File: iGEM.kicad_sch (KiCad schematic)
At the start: 33 parts, among them IC1 TMCS1107A1BQDRQ1, IC2 TMCS1107A1BQDRQ1, IC3 MCP4642-502E_UN, J1 Conn_01x02, J2 Conn_01x02, J3 Conn_01x02, J4 Conn_01x02, Q1 TIP122, Q2 TIP122, Q3 IRF4905, Q4 D44VH, Q5 IRF4905, Q6 D44VH, U1 ADC101C021CIMK, U2 ADC101C021CIMK, U3 PCA9536D, U4 ICL7667

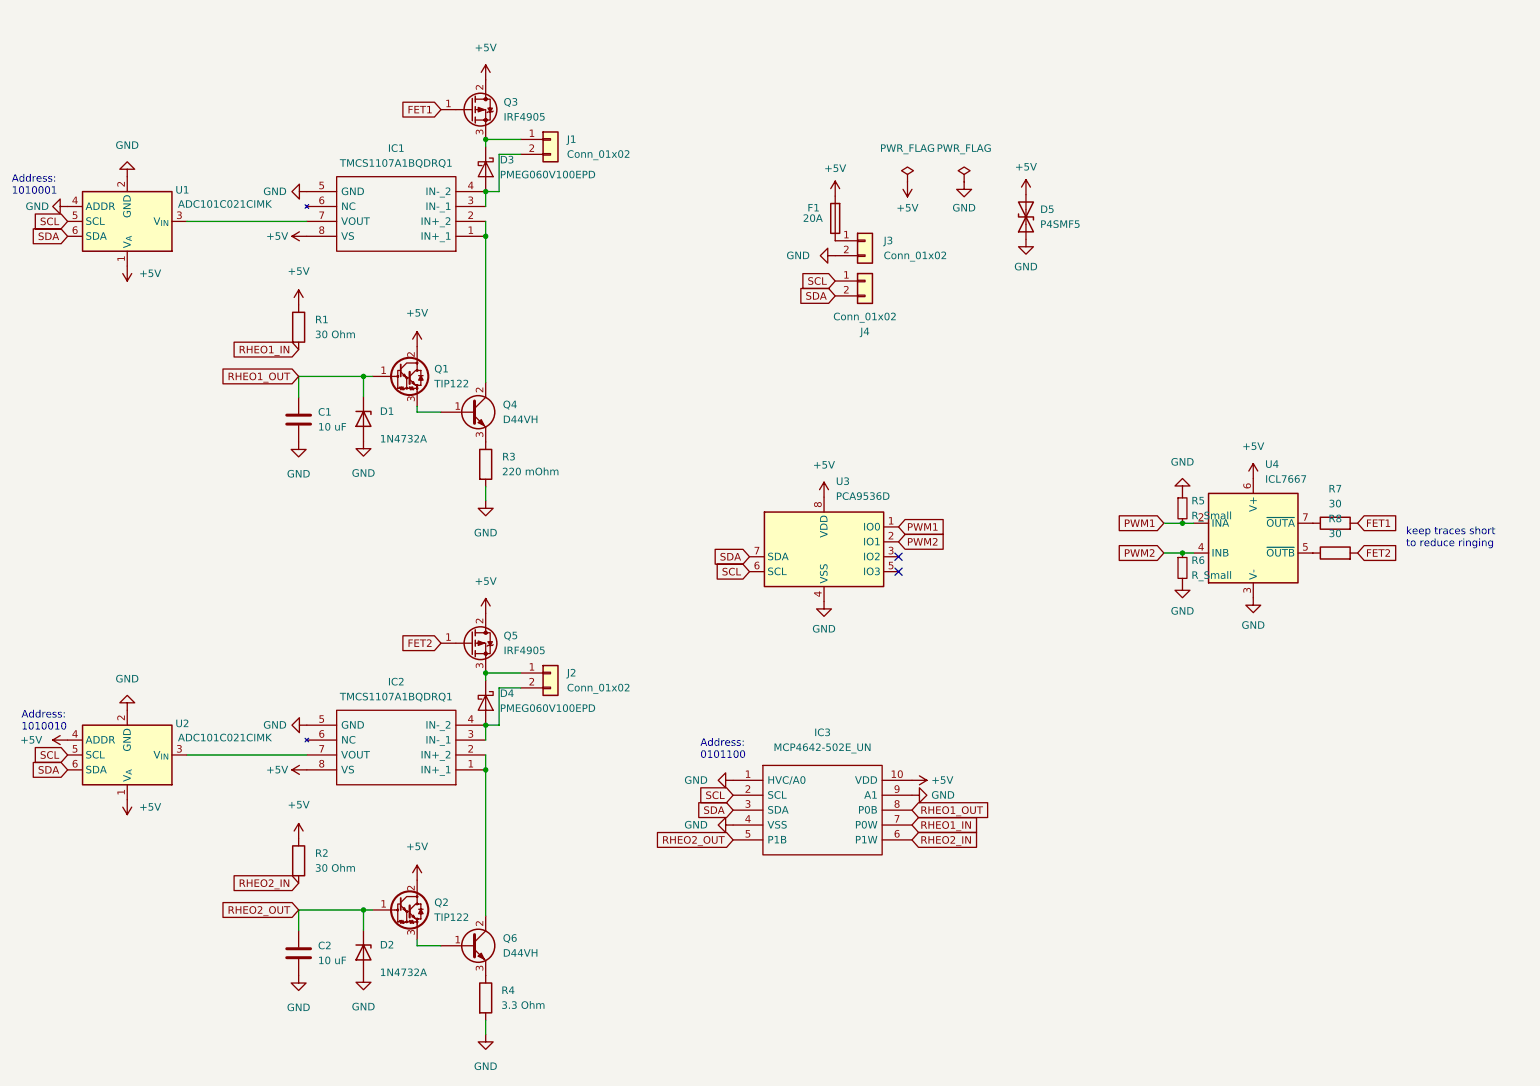
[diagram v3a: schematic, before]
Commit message: Schematics capture complete. Added footprints and DigiKey part numbers
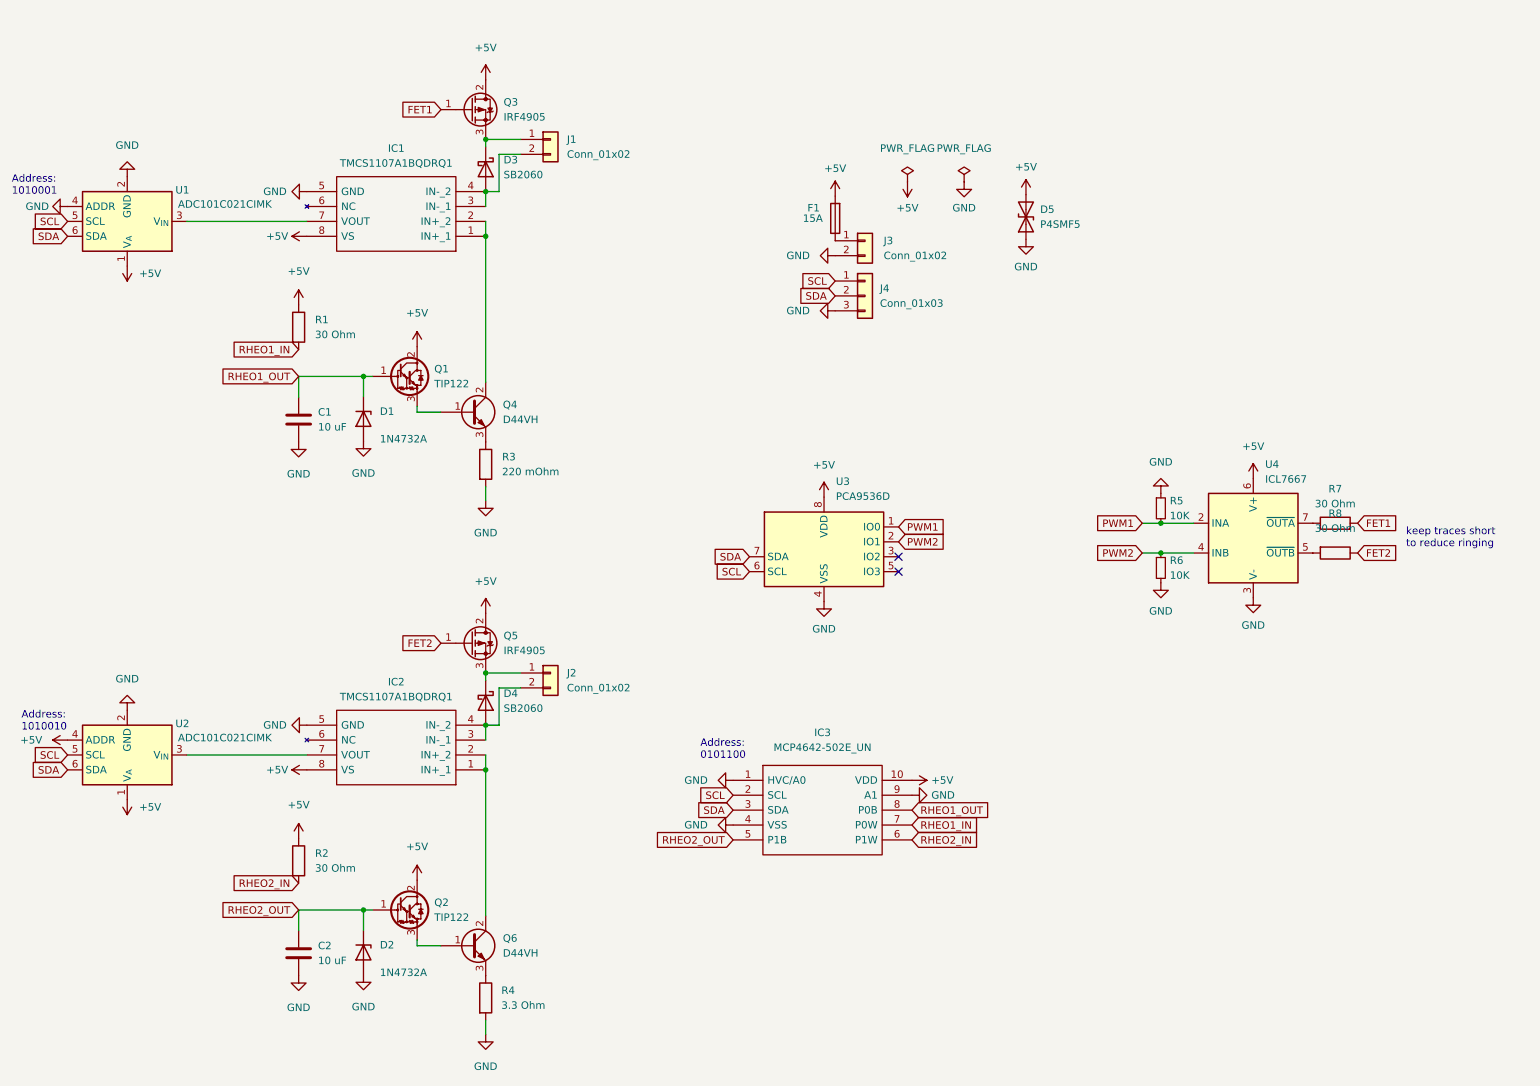
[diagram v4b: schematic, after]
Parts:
- removed D3, D4: PMEG060V100EPD, Package_TO_SOT_SMD:Nexperia_CFP15_SOT-1289, symbol Diode:PMEG060V100EPD
- removed J4: Conn_01x02, symbol Connector_Generic:Conn_01x02
- added D3, D4: SB2060, Diode_THT:D_DO-201AD_P15.24mm_Horizontal, symbol Device:D_Schottky
- added J4: Conn_01x03, Connector_JST:JST_XH_B3B-XH-AM_1x03_P2.50mm_Vertical, symbol Connector_Generic:Conn_01x03
- C1, C2: footprint (none) -> Capacitor_SMD:C_0805_2012Metric_Pad1.18x1.45mm_HandSolder; DigiKey (none) -> 399-C0805C106K8PAC7800CT-ND
- D1, D2: DigiKey (none) -> 1N4732AFSCT-ND
- D5: footprint (none) -> Diode_SMD:D_SOD-123F; DigiKey (none) -> 1655-P4SMF5.0CACT-ND
- F1: value 20A -> 15A; footprint (none) -> Fuse:Fuseholder_Blade_Mini_Keystone_3568; DigiKey (none) -> 36-3568-15-ND
- IC1: footprint TMCS1107A1BQDRQ1:SOIC127P600X175-8N -> Package_SO:SOIC-8_3.9x4.9mm_P1.27mm; DigiKey (none) -> 296-TMCS1107A1BQDRQ1CT-ND
- IC2: DigiKey (none) -> 296-TMCS1107A1BQDRQ1CT-ND
- IC3: DigiKey (none) -> MCP4642-502E/UN-ND
- J1, J2: footprint (none) -> TerminalBlock:TerminalBlock_bornier-2_P5.08mm; DigiKey (none) -> 102-6218-ND
- J3: footprint (none) -> 8PCV-02-006:8PCV02006; DigiKey (none) -> A98460-ND
- Q1, Q2: DigiKey (none) -> TIP122GOS-ND
- Q3, Q5: DigiKey (none) -> IRF4905PBF-ND
- Q4, Q6: DigiKey (none) -> D44VH10GOS-ND
- R1, R2: footprint (none) -> Capacitor_SMD:C_0805_2012Metric_Pad1.18x1.45mm_HandSolder; DigiKey (none) -> RMCF0805FT30R0CT-ND
- R3: footprint (none) -> TerminalBlock:TerminalBlock_bornier-2_P5.08mm; DigiKey (none) -> A102180-ND
- R4: footprint (none) -> TerminalBlock:TerminalBlock_bornier-2_P5.08mm; DigiKey (none) -> A102423-ND
- R5, R6: value R_Small -> 10K; footprint (none) -> Capacitor_SMD:C_0805_2012Metric_Pad1.18x1.45mm_HandSolder; DigiKey (none) -> RMCF0805FT10K0CT-ND
- R7, R8: value 30 -> 30 Ohm; footprint (none) -> Capacitor_SMD:C_0805_2012Metric_Pad1.18x1.45mm_HandSolder; DigiKey (none) -> RMCF0805FT30R0CT-ND
- U1, U2: DigiKey (none) -> ADC101C021CIMK/NOPBCT-ND
- U3: DigiKey (none) -> 296-21765-1-ND
- U4: footprint (none) -> Package_SO:SOIC-8_3.9x4.9mm_P1.27mm; DigiKey (none) -> ICL7667EBA+-ND
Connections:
- net FET2: now also R8.1; no longer R8.2
- net GND: now also J4.3 (Pin_3)
- net SCL: now also J4.1 (Pin_1)
- net SDA: now also J4.2 (Pin_2)
- net at J1.1 (Pin_1), Q3.3 (S): now also D3.1 (K)
- net at IC1.3 (IN-_1), IC1.4 (IN-_2), J1.2 (Pin_2): now also D3.2 (A)
- net at IC2.3 (IN-_1), IC2.4 (IN-_2), J2.2 (Pin_2): now also D4.2 (A)
- net at J2.1 (Pin_1), Q5.3 (S): now also D4.1 (K)
- net at U4.5 (~{OUTB}): now also R8.2; no longer R8.1
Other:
- moved on the sheet: R5, R6, R8

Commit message: layout draft complete
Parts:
- removed D5: P4SMF5, Diode_SMD:D_SOD-123F, symbol Device:D_TVS
- added C10, C6, C7, C8: 4.7 uF, Capacitor_Tantalum_SMD:CP_EIA-3528-21_Kemet-B_Pad1.50x2.35mm_HandSolder, symbol Device:C_Polarized
- added C11, C3, C4, C5, C9: 0.1 uF, Capacitor_SMD:C_0805_2012Metric_Pad1.18x1.45mm_HandSolder, symbol Device:C
- added H1, H2, H3, H4: MH, MountingHole:MountingHole_5.3mm_M5_DIN965_Pad, symbol Mechanical:MountingHole_Pad
- added HS1, HS2: Heatsink, Heatsink:Heatsink_AAVID_576802B03900G, symbol Mechanical:Heatsink_Pad
- added M1: Fan, Connector_JST:JST_XH_B2B-XH-AM_1x02_P2.50mm_Vertical, symbol Motor:Fan
- added R10, R9: 5K, Resistor_SMD:R_0805_2012Metric_Pad1.20x1.40mm_HandSolder, symbol Device:R
- C1, C2: value 10 uF -> 0.1 uF; DigiKey 399-C0805C106K8PAC7800CT-ND -> (none)
- D3, D4: footprint Diode_THT:D_DO-201AD_P15.24mm_Horizontal -> Diode_THT:D_DO-201AD_P12.70mm_Horizontal
- J4: DigiKey 455-2250-ND -> 455-2231-ND
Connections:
- net +5V: now also C1.1, C2.1, C10.1, C11.1, C3.1, C4.1, C5.1, C6.1, C7.1, C8.1, C9.1, M1.1 (+), R10.1, R9.1
- net GND: now also C10.2, C11.2, C3.2, C4.2, C5.2, C6.2, C7.2, C8.2, C9.2, H1.1, H2.1, H3.1, H4.1, M1.2 (-)
- net RHEO1_OUT: no longer C1.1
- net RHEO2_OUT: no longer C2.1
- net SCL: now also R9.2
- net SDA: now also R10.2
- net at D3.2 (A), J1.2 (Pin_2): now also IC1.1 (IN+_1), IC1.2 (IN+_2); no longer IC1.3 (IN-_1), IC1.4 (IN-_2)
- net at IC2.1 (IN+_1), IC2.2 (IN+_2): now also D4.2 (A), J2.2 (Pin_2); no longer Q6.2 (C)
- net at IC2.3 (IN-_1), IC2.4 (IN-_2): now also Q6.2 (C), HS2.1; no longer D4.2 (A), J2.2 (Pin_2)
- new net: HS1.1, IC1.3 (IN-_1), IC1.4 (IN-_2), Q4.2 (C)
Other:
- moved on the sheet: F1, IC1, IC2, IC3, J3, J4, U1, U2

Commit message: updated DigiKey part numbers and value of i2c pullups
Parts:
- C1, C11, C2, C3, C4, C5, C9: DigiKey (none) -> 399-C0805C104K8RAC7800CT-ND
- M1: DigiKey (none) -> 455-2879-ND
- R10, R9: value 5K -> 4.7K; DigiKey (none) -> RMCF0805FT4K70CT-ND
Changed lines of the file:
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@@
+      (effects (font (size 1.27 1.27)) hide)
+    )
+    (property "DigiKey" "399-C0805C104K8RAC7800CT-ND" (id 4) (at 172.466 88.773 0)
       (effects (font (size 1.27 1.27)) hide)
     )
@@
       (effects (font (size 1.27 1.27)) (justify left))
     )
-    (property "Value" "5K" (id 1) (at 255.778 51.8159 0)
+    (property "Value" "4.7K" (id 1) (at 255.778 51.8159 0)
       (effects (font (size 1.27 1.27)) (justify left))
     )
@@
     )
     (property "Datasheet" "~" (id 3) (at 253.873 50.546 0)
+      (effects (font (size 1.27 1.27)) hide)
+    )
+    (property "DigiKey" "RMCF0805FT4K70CT-ND" (id 4) (at 253.873 50.546 0)
       (effects (font (size 1.27 1.27)) hide)
     )
@@
     )
     (property "Datasheet" "~" (id 3) (at 242.443 82.169 0)
+      (effects (font (size 1.27 1.27)) hide)
+    )
+    (property "DigiKey" "399-C0805C104K8RAC7800CT-ND" (id 4) (at 242.443 82.169 0)
       (effects (font (size 1.27 1.27)) hide)
     )
@@
       (effects (font (size 1.27 1.27)) (justify left))
     )
-    (property "Value" "5K" (id 1) (at 263.017 51.8159 0)
+    (property "Value" "4.7K" (id 1) (at 263.017 51.8159 0)
       (effects (font (size 1.27 1.27)) (justify left))
     )
@@
     )
     (property "Datasheet" "~" (id 3) (at 260.35 50.546 0)
+      (effects (font (size 1.27 1.27)) hide)
+    )
+    (property "DigiKey" "RMCF0805FT4K70CT-ND" (id 4) (at 260.35 50.546 0)
       (effects (font (size 1.27 1.27)) hide)
     )
@@
       (effects (font (size 1.27 1.27)) hide)
     )
+    (property "DigiKey" "399-C0805C104K8RAC7800CT-ND" (id 4) (at 259.715 135.382 0)
+      (effects (font (size 1.27 1.27)) hide)
+    )
     (pin "1")
     (pin "2")
@@
     )
     (property "Datasheet" "~" (id 3) (at 128.905 31.369 0)
+      (effects (font (size 1.27 1.27)) hide)
+    )
+    (property "DigiKey" "399-C0805C104K8RAC7800CT-ND" (id 4) (at 128.905 31.369 0)
       (effects (font (size 1.27 1.27)) hide)
     )
@@
       (effects (font (size 1.27 1.27)) hide)
     )
+    (property "DigiKey" "399-C0805C104K8RAC7800CT-ND" (id 4) (at 128.651 122.174 0)
+      (effects (font (size 1.27 1.27)) hide)
+    )
     (pin "1")
     (pin "2")
@@
       (effects (font (size 1.27 1.27)) hide)
     )
+    (property "DigiKey" "455-2879-ND" (id 4) (at 263.398 27.178 0)
+      (effects (font (size 1.27 1.27)) hide)
+    )
     (pin "1")
     (pin "2")
@@
       (effects (font (size 1.27 1.27)) hide)
     )
+    (property "DigiKey" "399-C0805C104K8RAC7800CT-ND" (id 4) (at 179.197 123.444 0)
+      (effects (font (size 1.27 1.27)) hide)
+    )
     (pin "1")
     (pin "2")
@@
     )
     (property "Datasheet" "~" (id 3) (at 179.197 32.131 0)
+      (effects (font (size 1.27 1.27)) hide)
+    )
+    (property "DigiKey" "399-C0805C104K8RAC7800CT-ND" (id 4) (at 179.197 32.131 0)
       (effects (font (size 1.27 1.27)) hide)
     )
@@
     )
     (path "/1077e872-3c2a-4d54-b8f8-6275676956e2"
-      (reference "R9") (unit 1) (value "5K") (footprint "Resistor_SMD:R_0805_2012Metric_Pad1.20x1.40mm_HandSolder")
+      (reference "R9") (unit 1) (value "4.7K") (footprint "Resistor_SMD:R_0805_2012Metric_Pad1.20x1.40mm_HandSolder")
     )
     (path "/3f4af9bf-6e51-4fa2-939e-94b56f8a6a0c"
-      (reference "R10") (unit 1) (value "5K") (footprint "Resistor_SMD:R_0805_2012Metric_Pad1.20x1.40mm_HandSolder")
+      (reference "R10") (unit 1) (value "4.7K") (footprint "Resistor_SMD:R_0805_2012Metric_Pad1.20x1.40mm_HandSolder")
     )
     (path "/69a61c1d-1543-4184-a789-f583b0735f7e"

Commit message: Added PCA9536D address
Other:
- note added: "Address: 1000001"
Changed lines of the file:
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@@
     (stroke (width 0) (type default) (color 0 0 0 0))
+  )
+  (text "Address:\n1000001" (at 145.034 97.409 0)
+    (effects (font (size 1.27 1.27)) (justify left bottom))
   )
   (text "keep traces short\nto reduce ringing" (at 255.778 105.029 0)

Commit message: mounting holes no longer connected to signal ground because the chassis will be connected to true earth
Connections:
- net GND: no longer H1.1, H2.1, H3.1, H4.1
- no-connect marks 2 -> 6
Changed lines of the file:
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@@
   (junction (at 78.105 75.692) (diameter 0) (color 0 0 0 0)
   )
+  (no_connect (at 220.98 24.511))
+  (no_connect (at 228.727 24.638))
+  (no_connect (at 236.093 24.638))
+  (no_connect (at 243.84 24.765))
   (no_connect (at 169.291 106.426))
   (no_connect (at 169.291 108.966))
@@
     (pin "2")
     (pin "3")
-  )
-  (symbol (lib_id "power:GND") (at 220.98 24.511 0) (unit 1)
-    (in_bom yes) (on_board yes) (fields_autoplaced)
-    (property "Reference" "#PWR08" (id 0) (at 220.98 30.861 0)
-      (effects (font (size 1.27 1.27)) hide)
-    )
-    (property "Value" "GND" (id 1) (at 220.98 29.21 0))
-    (property "Footprint" "" (id 2) (at 220.98 24.511 0)
-      (effects (font (size 1.27 1.27)) hide)
-    )
-    (property "Datasheet" "" (id 3) (at 220.98 24.511 0)
-      (effects (font (size 1.27 1.27)) hide)
-    )
-    (pin "1")
-  )
-  (symbol (lib_id "power:GND") (at 243.84 24.765 0) (unit 1)
-    (in_bom yes) (on_board yes) (fields_autoplaced)
-    (property "Reference" "#PWR030" (id 0) (at 243.84 31.115 0)
-      (effects (font (size 1.27 1.27)) hide)
-    )
-    (property "Value" "GND" (id 1) (at 243.84 29.464 0))
-    (property "Footprint" "" (id 2) (at 243.84 24.765 0)
-      (effects (font (size 1.27 1.27)) hide)
-    )
-    (property "Datasheet" "" (id 3) (at 243.84 24.765 0)
-      (effects (font (size 1.27 1.27)) hide)
-    )
-    (pin "1")
   )
   (symbol (lib_id "power:GND") (at 156.591 114.046 0) (unit 1)
@@
     (pin "1")
   )
-  (symbol (lib_id "power:GND") (at 228.727 24.638 0) (unit 1)
-    (in_bom yes) (on_board yes) (fields_autoplaced)
-    (property "Reference" "#PWR010" (id 0) (at 228.727 30.988 0)
-      (effects (font (size 1.27 1.27)) hide)
-    )
-    (property "Value" "GND" (id 1) (at 228.727 29.337 0))
-    (property "Footprint" "" (id 2) (at 228.727 24.638 0)
-      (effects (font (size 1.27 1.27)) hide)
-    )
-    (property "Datasheet" "" (id 3) (at 228.727 24.638 0)
-      (effects (font (size 1.27 1.27)) hide)
-    )
-    (pin "1")
-  )
   (symbol (lib_id "Device:R") (at 98.933 90.678 0) (unit 1)
     (in_bom yes) (on_board yes) (fields_autoplaced)
@@
     (pin "1")
     (pin "2")
-  )
-  (symbol (lib_id "power:GND") (at 236.093 24.638 0) (unit 1)
-    (in_bom yes) (on_board yes) (fields_autoplaced)
-    (property "Reference" "#PWR029" (id 0) (at 236.093 30.988 0)
-      (effects (font (size 1.27 1.27)) hide)
-    )
-    (property "Value" "GND" (id 1) (at 236.093 29.337 0))
-    (property "Footprint" "" (id 2) (at 236.093 24.638 0)
-      (effects (font (size 1.27 1.27)) hide)
-    )
-    (property "Datasheet" "" (id 3) (at 236.093 24.638 0)
-      (effects (font (size 1.27 1.27)) hide)
-    )
-    (pin "1")
   )
   (symbol (lib_id "Device:R") (at 243.713 105.791 270) (unit 1)
@@
       (reference "#PWR07") (unit 1) (value "+5V") (footprint "")
     )
-    (path "/042a7d63-7b80-4917-a290-31657c7b8a48"
-      (reference "#PWR08") (unit 1) (value "GND") (footprint "")
-    )
     (path "/8a23fdf2-c219-420d-8e03-42ba1d0d99f7"
       (reference "#PWR09") (unit 1) (value "+5V") (footprint "")
     )
-    (path "/49c793d3-4f83-490e-b7ed-63c29414cf6c"
-      (reference "#PWR010") (unit 1) (value "GND") (footprint "")
-    )
     (path "/eda42a90-3930-4604-9893-d06fe181b339"
       (reference "#PWR011") (unit 1) (value "GND") (footprint "")
@@
       (reference "#PWR028") (unit 1) (value "+5V") (footprint "")
     )
-    (path "/cbee4b78-8611-4849-a049-7cb3325424e4"
-      (reference "#PWR029") (unit 1) (value "GND") (footprint "")
-    )
-    (path "/06e2f41f-e054-44cb-a77d-739511c028ea"
-      (reference "#PWR030") (unit 1) (value "GND") (footprint "")
-    )
     (path "/8a9f4748-d262-4938-868b-9e1766b551d3"
